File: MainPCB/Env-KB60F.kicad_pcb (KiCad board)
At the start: 2 copper layers, 283 x 126.5 mm, 145 parts, among them J1 TP3 Pad, J2 TP2 Pad, SW1 EVQ-P7A01P, U1 Pico

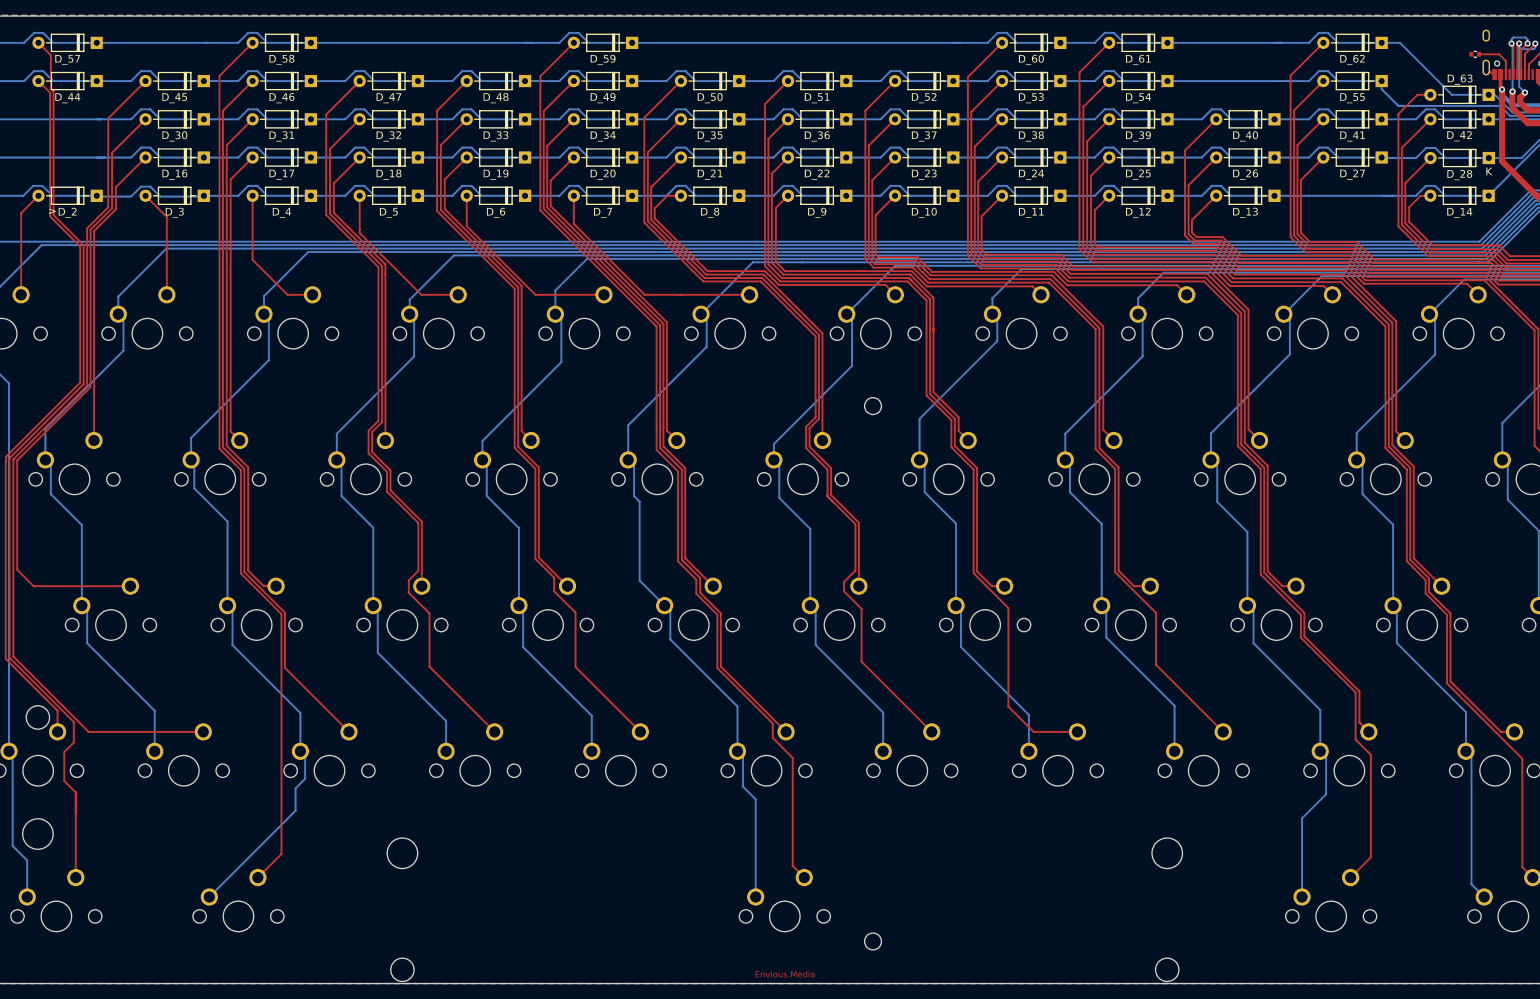
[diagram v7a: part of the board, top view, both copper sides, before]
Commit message: reorganize folder/files, added triple spacebar
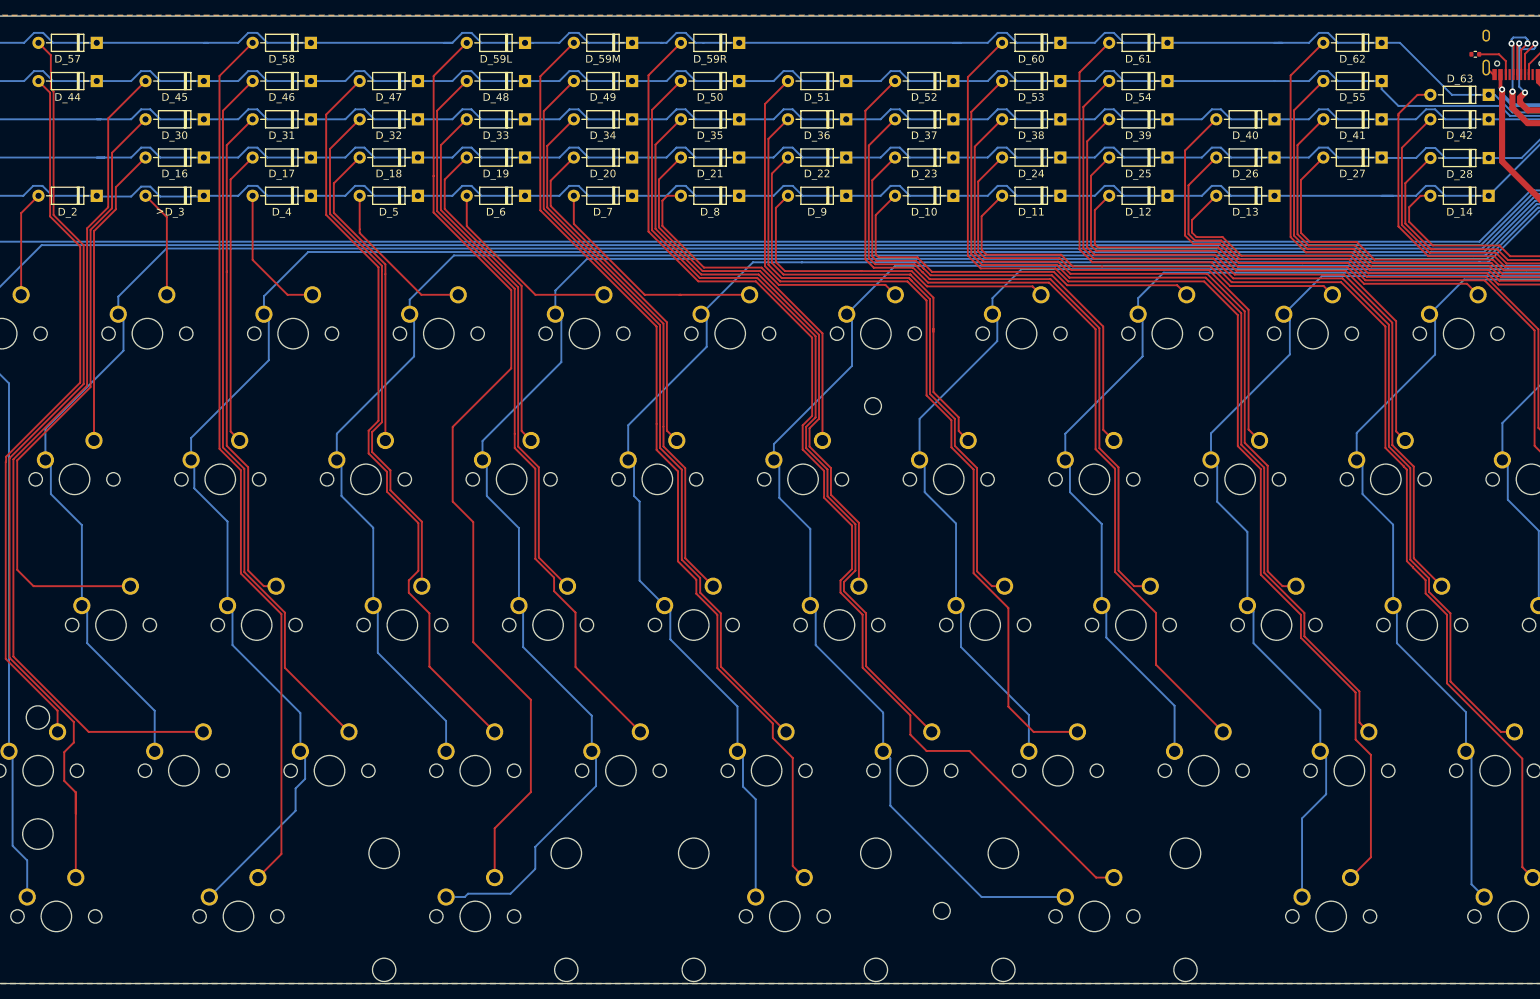
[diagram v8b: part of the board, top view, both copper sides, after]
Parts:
- added D_59L: D, Diode_THT:D_DO-35_SOD27_P7.62mm_Horizontal, F.Cu at (173.0, 36.5)
- added D_59R: D, Diode_THT:D_DO-35_SOD27_P7.62mm_Horizontal, F.Cu at (201.0, 36.5)
- added K_610: KEYSW, MX_Only:MXOnly-2U-ReversedStabilizers-NoLED, F.Cu at (166.5, 150.7)
- added K_612: KEYSW, MX_Only:MXOnly-2U-ReversedStabilizers-NoLED, F.Cu at (247.4, 150.7)
- K_61: footprint MX_Only:MXOnly-6.25U-ReversedStabilizers-NoLED -> MX_Only:MXOnly-2.25U-ReversedStabilizers-NoLED
- moved H1 9.85 mm to (227.5, 150.0)
- renumbered D_59 to D_59M
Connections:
- USB1 pad 3: Net-(USB1-Pad3) -> (no net)
- USB1 pad 9: Net-(USB1-Pad9) -> (no net)
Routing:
- net Net-(D_591-Pad2): track 0.00 -> 147.4 mm
- net Net-(D_590-Pad2): track 0.00 -> 124.5 mm
- net col7: track 169.6 -> 204.9 mm
- net col5: track 247.5 -> 279.6 mm
- net row4: track 223.4 -> 225.7 mm
- net Net-(D_50-Pad2): track 110.5 -> 108.5 mm
- net Net-(D_8-Pad2): track 41.0 -> 40.2 mm
- net Net-(D_21-Pad2): track 52.3 -> 51.5 mm
- net Net-(D_35-Pad2): track 79.7 -> 78.9 mm
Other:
- board text removed: "Envious.Media"
